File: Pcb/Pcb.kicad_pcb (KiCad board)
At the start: 2 copper layers, 152.3 x 104.7 mm, 129 parts, among them J1 ISP, J2 TRRS, Q1 2N7002, SW1 SW_Push, SW10 SW_Push, SW11 SW_Push, SW12 SW_Push, SW13 SW_Push, SW14 SW_Push, SW15 SW_Push, SW16 SW_Push, SW17 SW_Push, SW18 SW_Push, SW19 SW_Push, SW2 SW2, SW20 SW_Push, SW21 SW_Push, SW22 SW_Push, SW23 SW_Push, SW24 SW_Push, SW25 SW_Push, SW26 SW_Push, SW27 SW_Push, SW28 SW_Push, SW29 SW_Push, SW3 SW_Push, SW4 SW_Push, SW5 SW_Push, SW6 SW_Push, SW7 SW_Push, SW8 SW_Push, SW9 SW_Push, U1 ProMicro

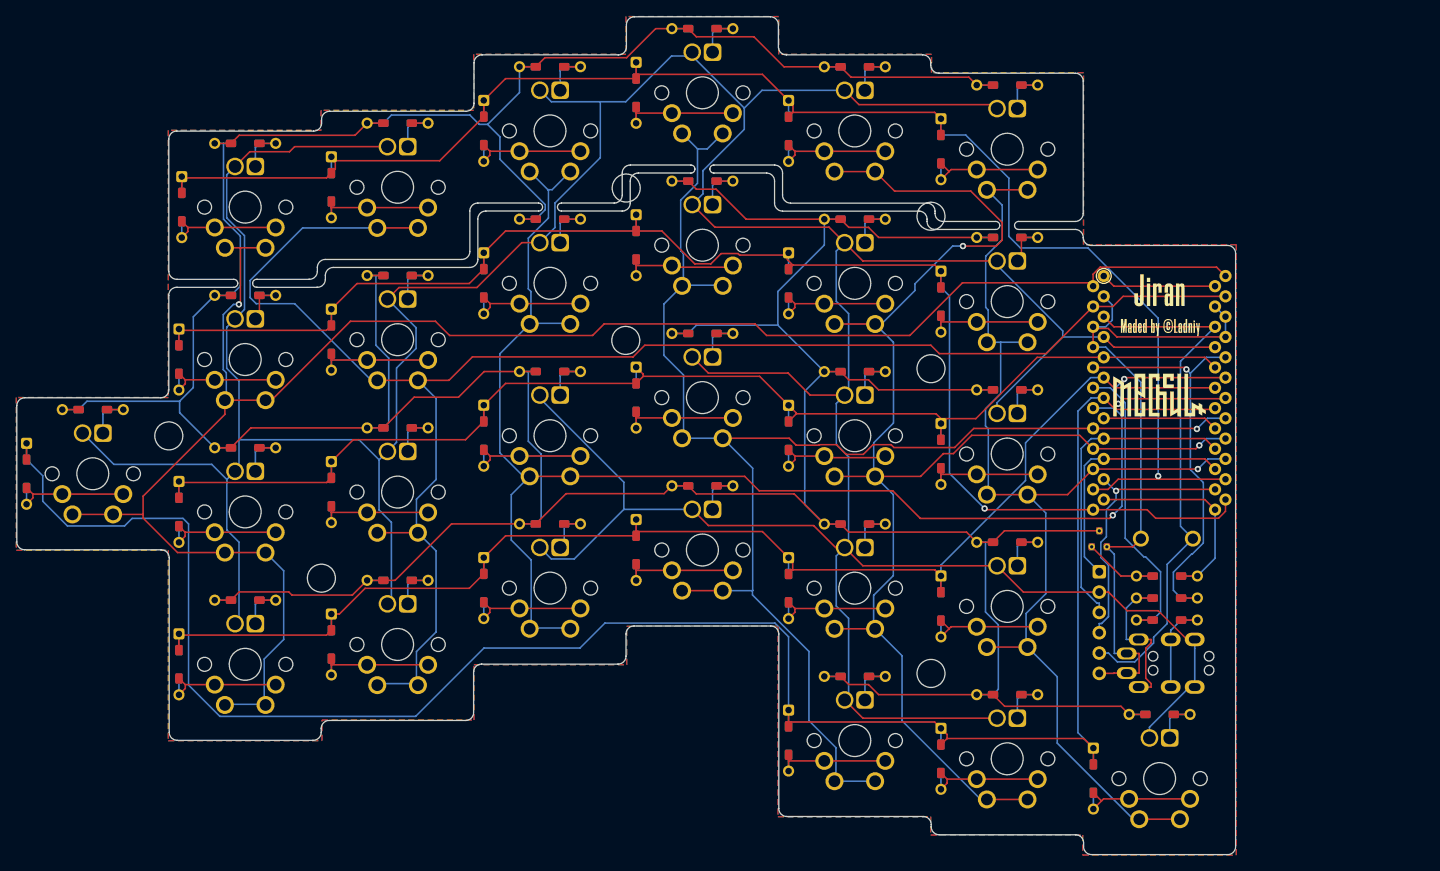
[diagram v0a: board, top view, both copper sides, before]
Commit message: Deleted track's
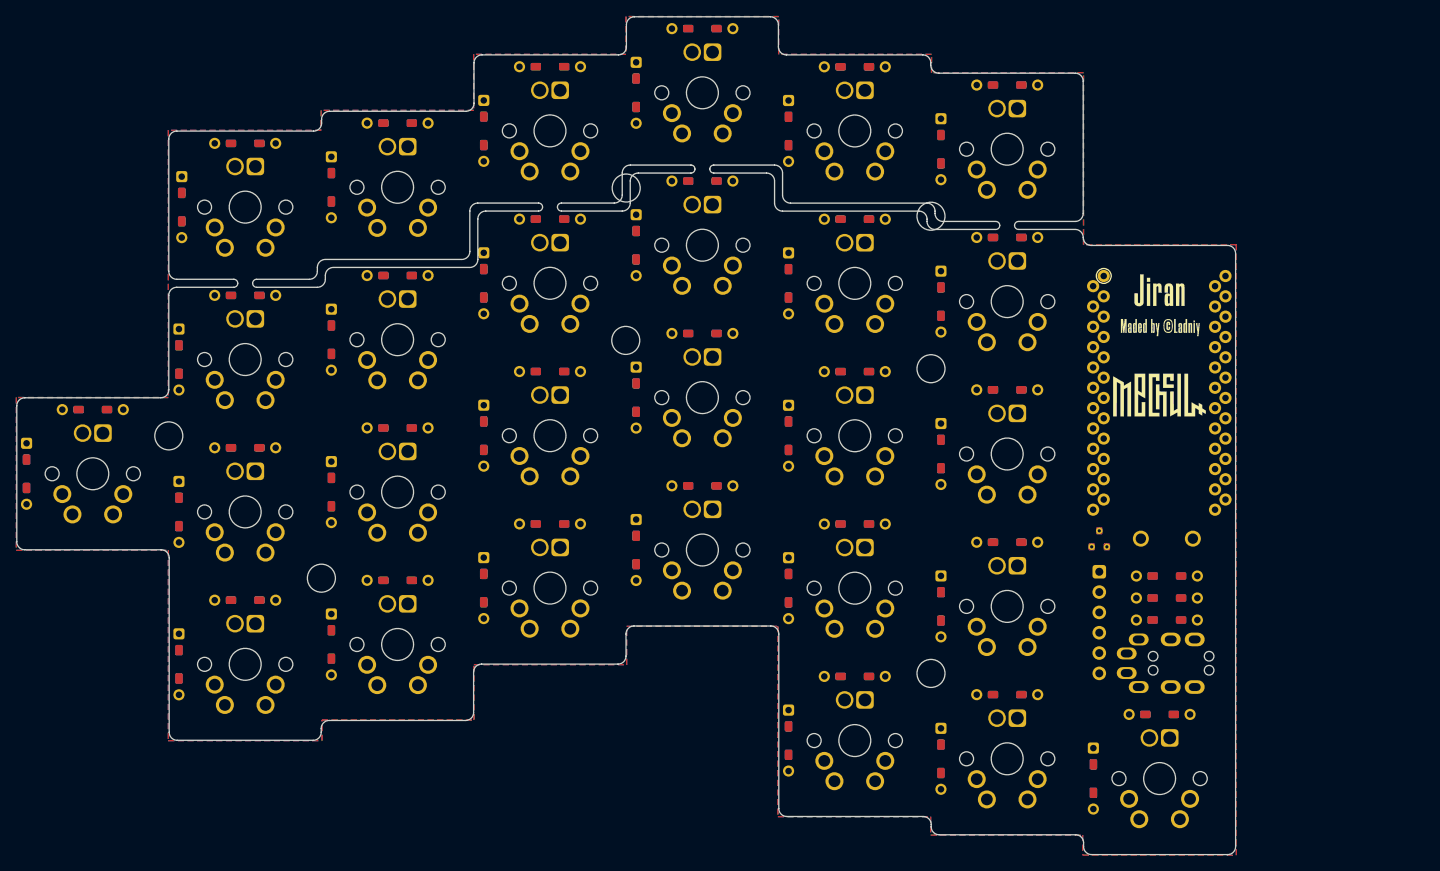
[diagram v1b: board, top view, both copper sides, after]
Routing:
- net /LEDOut: track 635.7 -> 0.00 mm
- net VCC: track 599.4 -> 0.00 mm
- net /rowE: track 254.2 -> 0.00 mm
- net /col0: track 232.7 -> 0.00 mm, vias 1 -> 0
- net /col1: track 209.5 -> 0.00 mm
- net /rowA: track 202.6 -> 0.00 mm, vias 1 -> 0
- net /rowB: track 188.0 -> 0.00 mm, vias 1 -> 0
- net /col2: track 185.0 -> 0.00 mm, vias 2 -> 0
- net /col3: track 184.5 -> 0.00 mm, vias 1 -> 0
- net /col4: track 183.5 -> 0.00 mm, vias 2 -> 0
- net /rowD: track 173.3 -> 0.00 mm
- net /rowC: track 163.1 -> 0.00 mm
- net /col5: track 141.7 -> 0.00 mm, vias 1 -> 0
- net GND: track 86.3 -> 0.00 mm
- net RST: track 66.7 -> 0.00 mm
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
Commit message: Moved diode
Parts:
- moved D1 0.35 mm to (97.4, 53.9)
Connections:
- R29 pad 1: Net-(R29-Pad1) -> SDA
- R29 pad 2: SDA -> VCC
- R30 pad 1: Net-(R30-Pad1) -> VCC
- U1 pad 5: Net-(R29-Pad1) -> SDA
- U1 pad 6: Net-(R30-Pad1) -> SCL

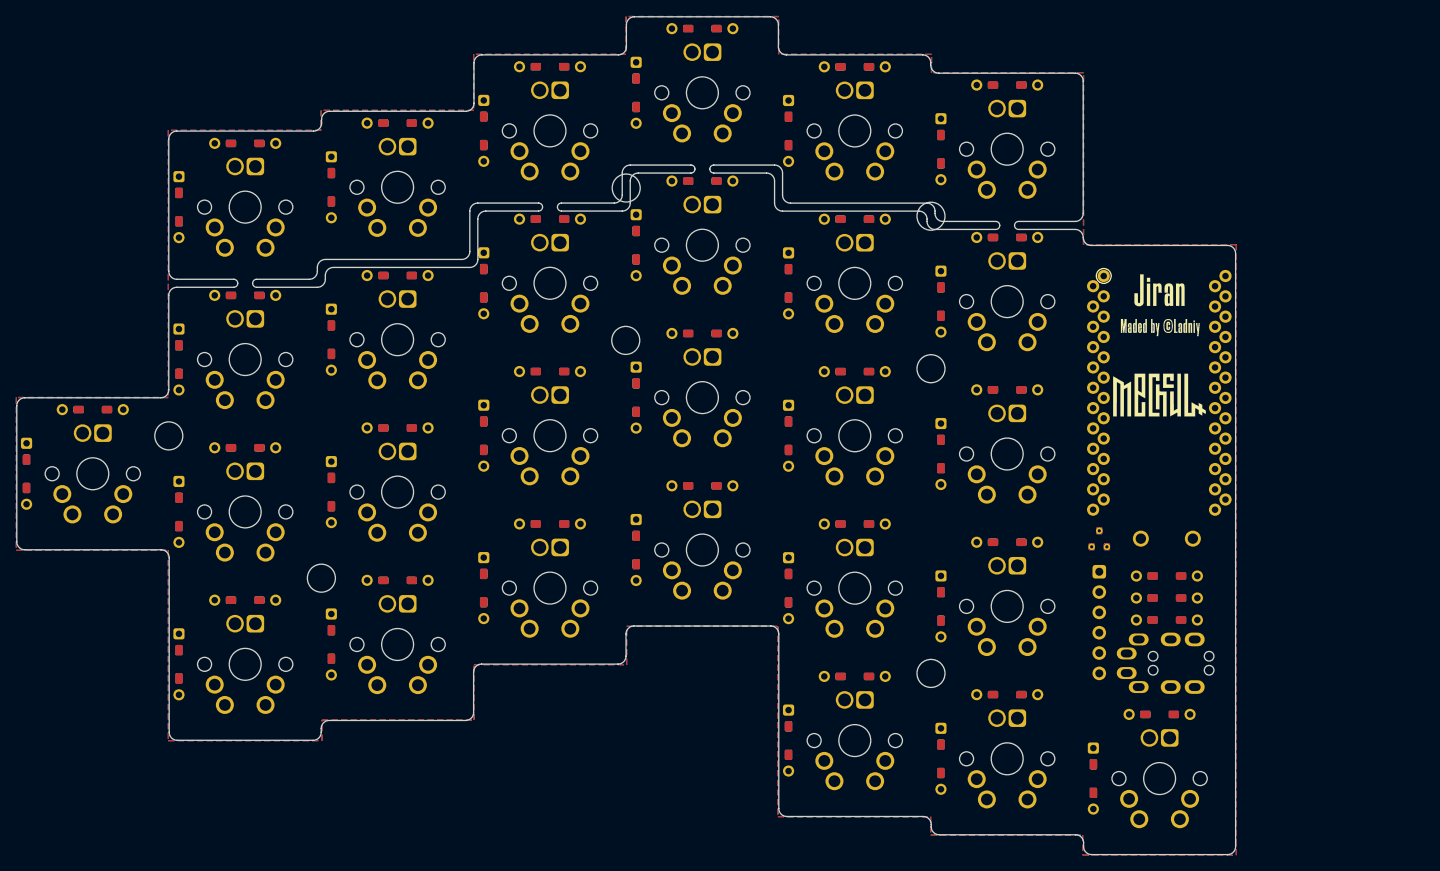
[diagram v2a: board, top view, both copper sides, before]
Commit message: Added support for Choc and Apls switche's
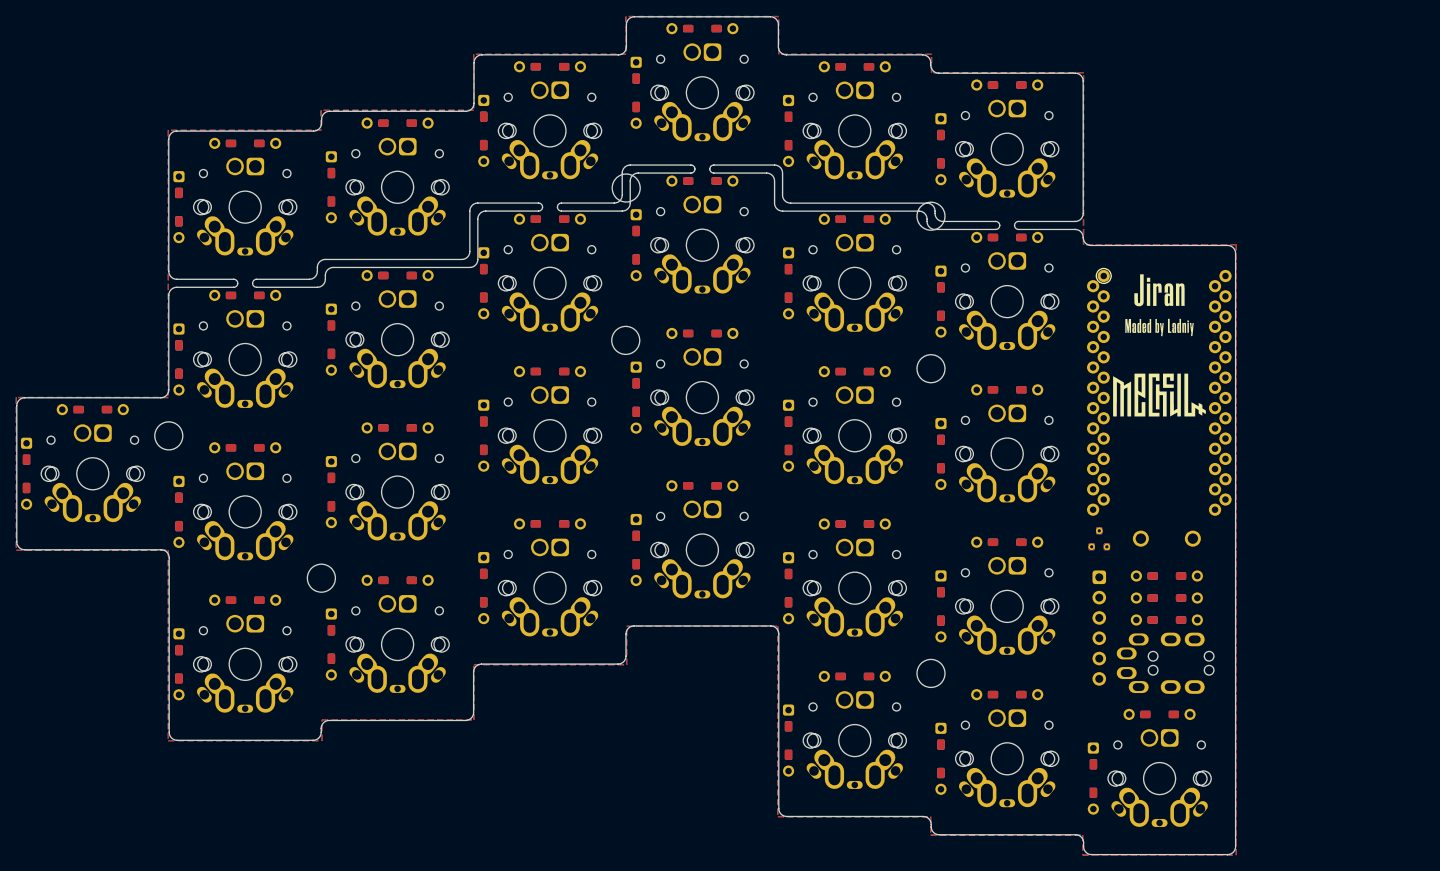
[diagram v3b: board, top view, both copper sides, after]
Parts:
- SW1, SW10, SW11, SW12, SW13, SW14, SW15, SW16, SW17, SW18, SW19, SW2, SW20, SW21, SW22, SW23, SW24, SW25, SW26, SW27, SW28, SW3, SW4, SW5, SW6, SW7, SW8, SW9: footprint Used_Footprints:MX_Two_Side -> 1symblos:cherry
- moved J1 0.69 mm to (212.5, 100.2)
- turned SW1 to 0 degrees
- turned SW10 to 0 degrees
- turned SW11 to 0 degrees
- turned SW12 to 0 degrees
- turned SW13 to 0 degrees
- turned SW14 to 0 degrees
- turned SW15 to 0 degrees
- turned SW16 to 0 degrees
- turned SW17 to 0 degrees
- turned SW18 to 0 degrees
- turned SW19 to 0 degrees
- turned SW2 to 0 degrees
- turned SW20 to 0 degrees
- turned SW21 to 0 degrees
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
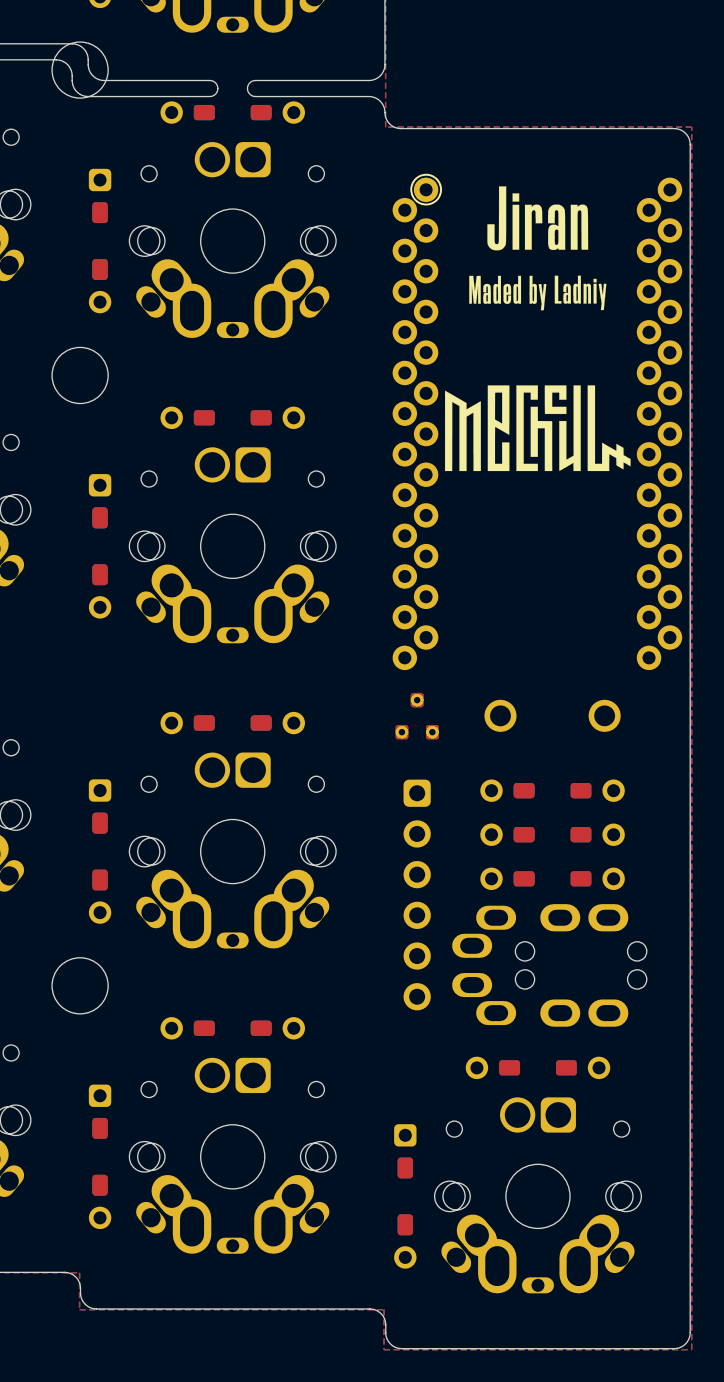
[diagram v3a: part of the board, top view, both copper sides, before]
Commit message: Moved some parts
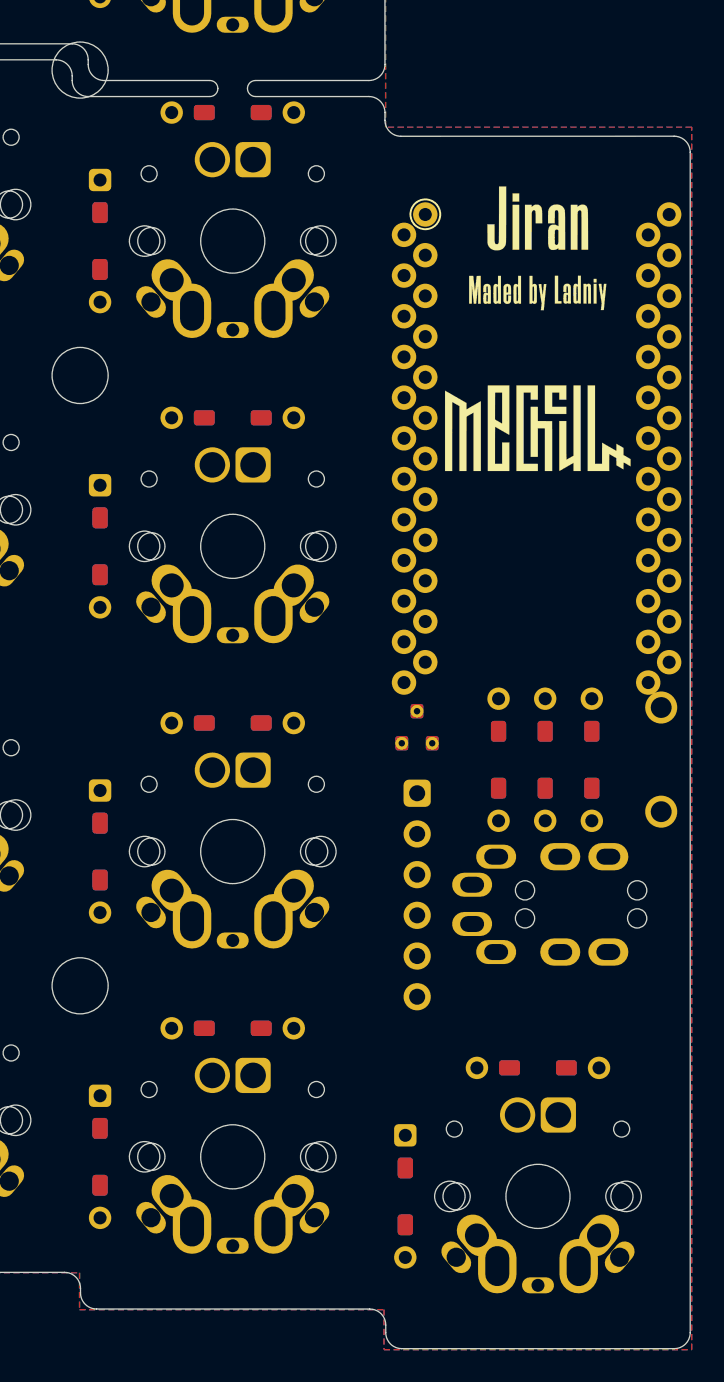
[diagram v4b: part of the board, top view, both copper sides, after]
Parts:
- moved R30 7.82 mm to (223.4, 98.1), turned to 270 degrees
- moved SW29 7.31 mm to (227.7, 98.1), turned to 90 degrees
- moved R29 4.70 mm to (220.5, 98.1), turned to 90 degrees
- moved R31 3.88 mm to (217.6, 98.1), turned to 90 degrees
- moved J2 3.81 mm to (221.3, 107.2)
- moved U1 1.54 mm to (220.5, 78.5)
- moved Q1 0.69 mm to (212.4, 96.1)
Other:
- outline, holes or cut-outs redrawn

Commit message: Updated footprints
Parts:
- removed G1, G2: LOGO, 1symblos:Jiran_Silk_Sign
- removed H4, H5, REFH1, REFH2, REFH3, REFH6, REFH7: MountHole, Used_Footprints:MountHole
- removed the J1 at (212.5, 100.2)
- added JP2: Jumper, 1kbd:jumper, F.Cu at (246.0, 106.0)
- added JP3: Jumper, 1kbd:jumper, F.Cu at (248.2, 106.0)
- added JP4: Jumper, 1kbd:jumper, F.Cu at (250.3, 106.0)
- added JP5: Jumper, 1kbd:jumper, F.Cu at (252.4, 106.0)
- J1: renamed from J2; footprint Used_Footprints:TRRS_2Side -> 1symblos:MJ-4PP-9_Dual
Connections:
- D54 pad 2: VCC -> /CAPS
- D55 pad 2: VCC -> /SCROLL
- D56 pad 2: VCC -> /NUM
- J1 pad A: GND -> Net-(J1-PadA)
- J1 pad B: VCC -> GND
- J1 pad C: SCL -> VCC
- J1 pad D: SDA -> Net-(J1-PadD)
- R26 pad 2: /LEDOut -> GND
- R27 pad 2: /LEDOut -> GND
- R28 pad 2: /LEDOut -> GND
- U1 pad 14: /MOSI -> /NUM
- U1 pad 15: /MISO -> /SCROLL
- U1 pad 16: /SCK -> /CAPS
